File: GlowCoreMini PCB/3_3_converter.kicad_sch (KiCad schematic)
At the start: 4 parts, among them U12 SPX3819M5-L-3-3_TR

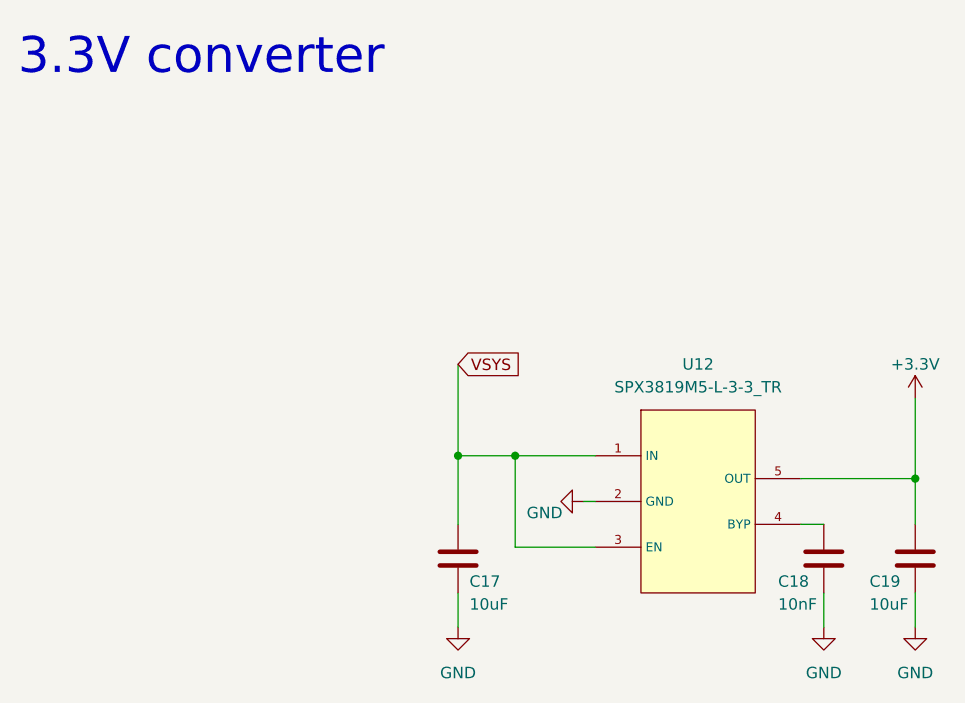
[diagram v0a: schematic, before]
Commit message: split up schematic
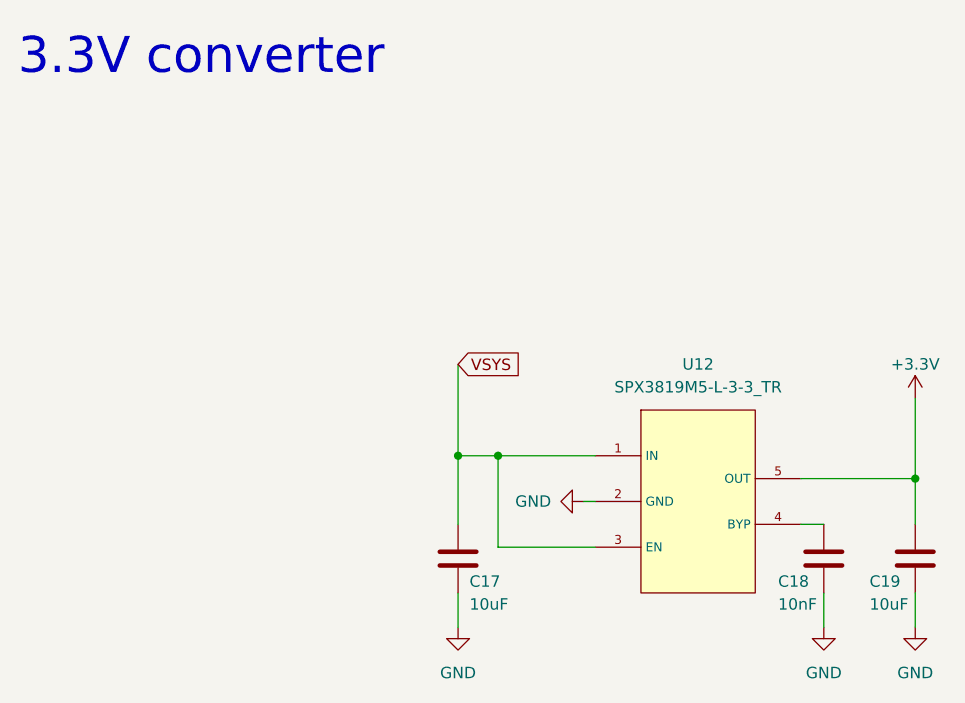
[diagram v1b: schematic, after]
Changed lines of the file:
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@@
 (kicad_sch (version 20230121) (generator eeschema)
   (paper "A4" portrait)
+  (junction (at 73.025 67.945) (diameter 0) (color 0 0 0 0)
+  )
   (junction (at 119.38 70.485) (diameter 0) (color 0 0 0 0)
-  )
-  (junction (at 74.93 67.945) (diameter 0) (color 0 0 0 0)
   )
   (junction (at 68.58 67.945) (diameter 0) (color 0 0 0 0)
@@
     (stroke (width 0) (type default))
   )
-  (wire (pts (xy 74.93 67.945) (xy 83.82 67.945))
-    (stroke (width 0) (type default))
-  )
   (wire (pts (xy 82.55 73.025) (xy 83.82 73.025))
     (stroke (width 0) (type default))
   )
-  (wire (pts (xy 74.93 78.105) (xy 74.93 67.945))
+  (wire (pts (xy 73.025 67.945) (xy 83.82 67.945))
+    (stroke (width 0) (type default))
+  )
+  (wire (pts (xy 73.025 78.105) (xy 73.025 67.945))
     (stroke (width 0) (type default))
   )
@@
     (stroke (width 0) (type default))
   )
-  (wire (pts (xy 68.58 67.945) (xy 74.93 67.945))
+  (wire (pts (xy 68.58 67.945) (xy 73.025 67.945))
     (stroke (width 0) (type default))
   )
@@
     (stroke (width 0) (type default))
   )
-  (wire (pts (xy 83.82 78.105) (xy 74.93 78.105))
+  (wire (pts (xy 83.82 78.105) (xy 73.025 78.105))
     (stroke (width 0) (type default))
   )
@@
       (effects (font (size 1.27 1.27)) hide)
     )
-    (property "Value" "GND" (at 76.2 74.295 90)
+    (property "Value" "GND" (at 74.93 73.025 90)
       (effects (font (size 1.27 1.27)) (justify left))
     )
